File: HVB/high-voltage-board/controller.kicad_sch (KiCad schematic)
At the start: 24 parts, among them J10 Conn_01x05, U4 LD1117S33TR_SOT223, U5 STM32F413CGUx, U6 MCP2551-I-SN, Y1 Crystal

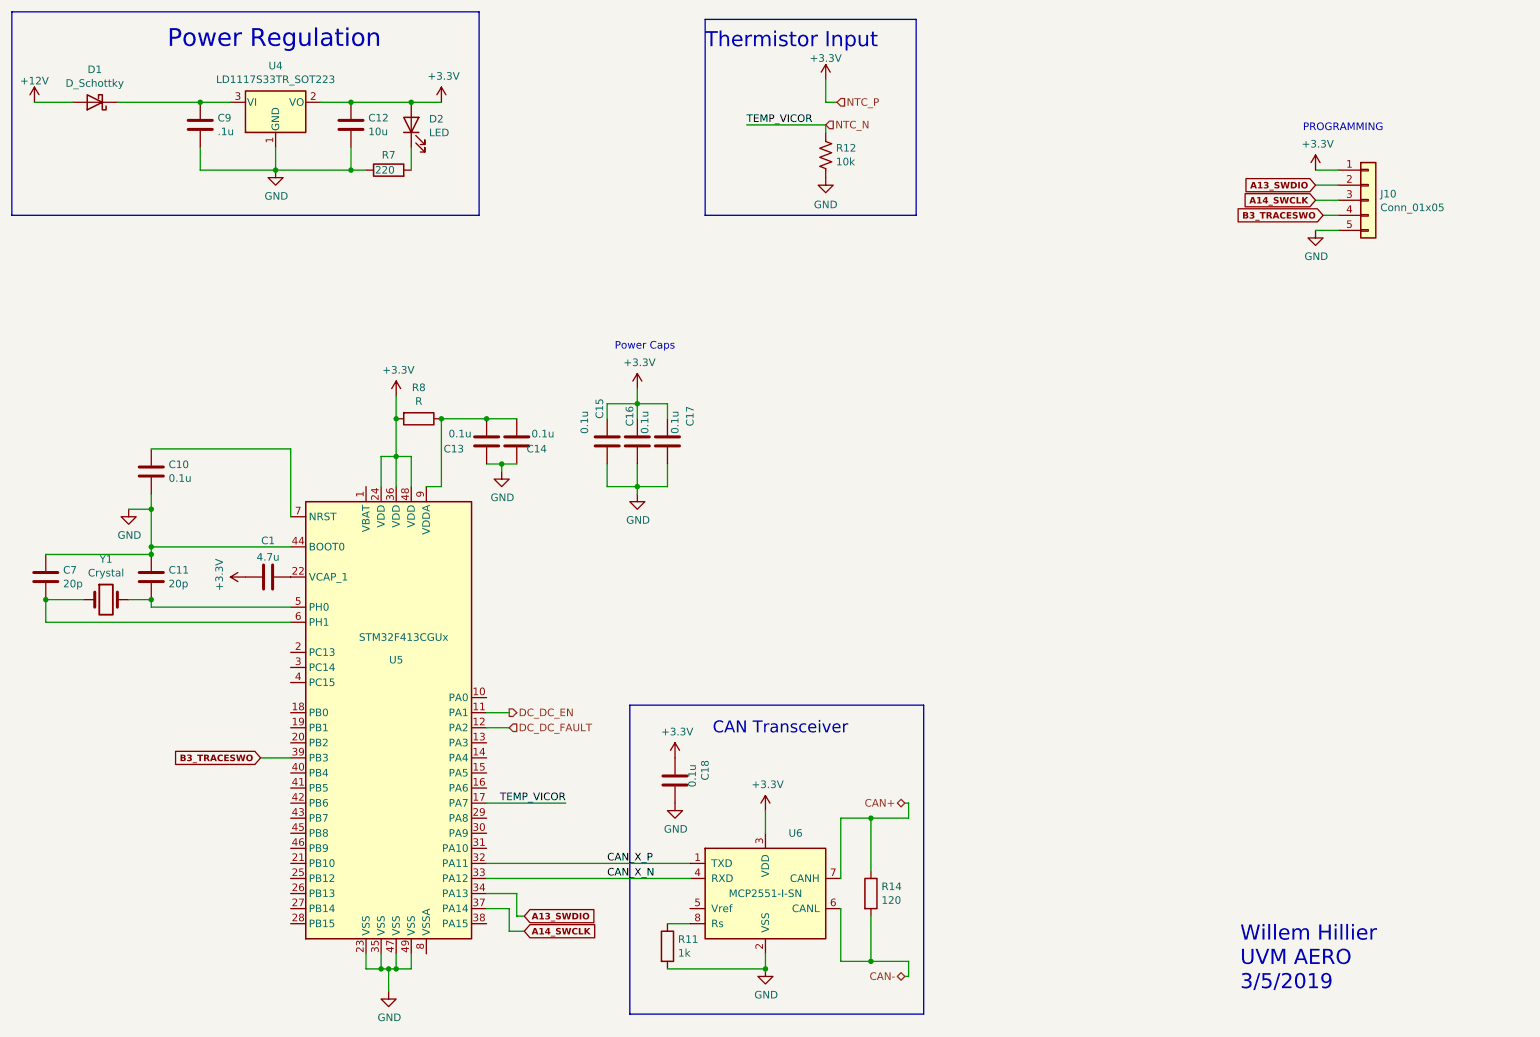
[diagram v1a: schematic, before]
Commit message: Major Review and Part Update
updating footprints, component values, layouts
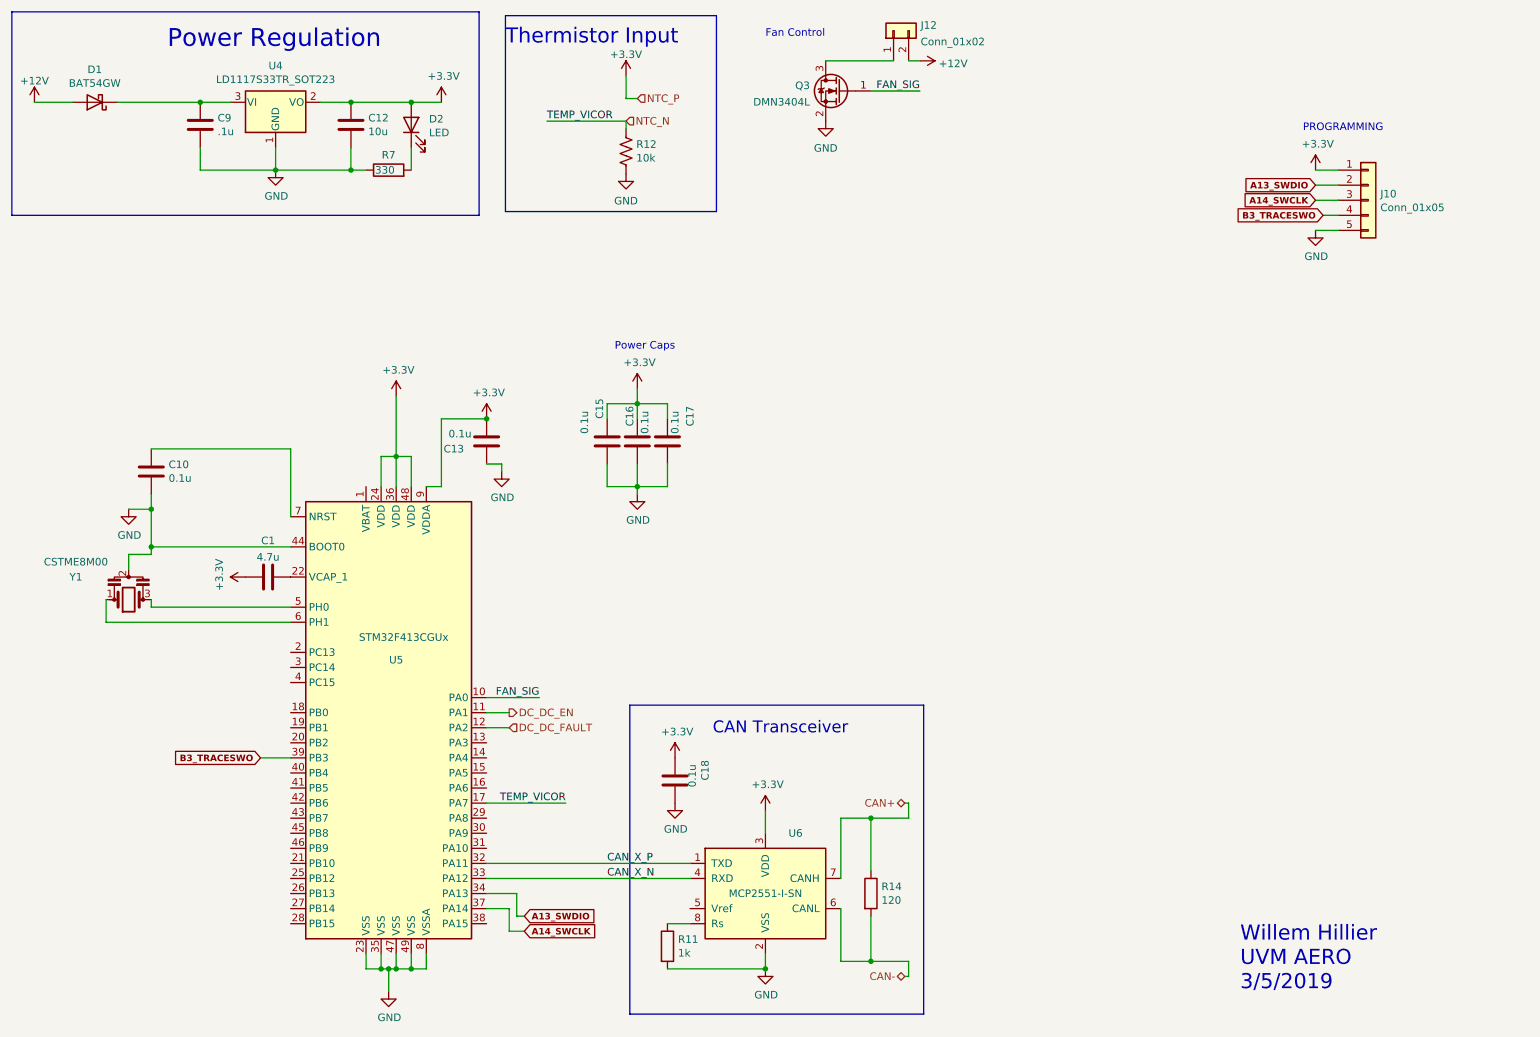
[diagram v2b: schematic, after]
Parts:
- removed C11, C7: 20p, Capacitor_SMD:C_0603_1608Metric_Pad1.08x0.95mm_HandSolder, symbol Device:C
- removed C14: 0.1u, Capacitor_SMD:C_0603_1608Metric_Pad1.08x0.95mm_HandSolder, symbol Device:C
- removed R8: R, Resistor_SMD:R_0603_1608Metric_Pad0.98x0.95mm_HandSolder, symbol Device:R
- removed Y1: Crystal, Crystal:Crystal_HC49-U_Vertical, symbol Device:Crystal
- added J12: Conn_01x02, Connector_JST:JST_XH_B2B-XH-A_1x02_P2.50mm_Vertical, symbol Connector_Generic:Conn_01x02
- added Q3: DMN3404L, Package_TO_SOT_SMD:SOT-23_Handsoldering, symbol Device:Q_NMOS_GSD
- added Y1: CSTME8M00, AERO_Footprints:Resonator_SMD_muRata_CSTxExxV-3Pin_3.0x1.1mm_HandSoldering, symbol Device:Resonator
- D1: value D_Schottky -> BAT54GW; footprint Diode_SMD:D_SMB_Handsoldering -> Diode_SMD:D_SOD-123
- R7: value 220 -> 330
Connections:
- net +12V: now also J12.2 (Pin_2)
- net +3V3: now also C13.2, U5.9 (VDDA)
- net GND: now also U5.8 (VSSA), Q3.2 (S), Y1.2
- net FAN_SIG: now reaches U5.10 (PA0)
- net FAN_SIG: now also Q3.1 (G)
- net at U5.5 (PH0): now also Y1.3
- net at U5.6 (PH1): now also Y1.1
- new net: J12.1 (Pin_1), Q3.3 (D)
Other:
- note added: "Fan Control"
- moved on the sheet: R12

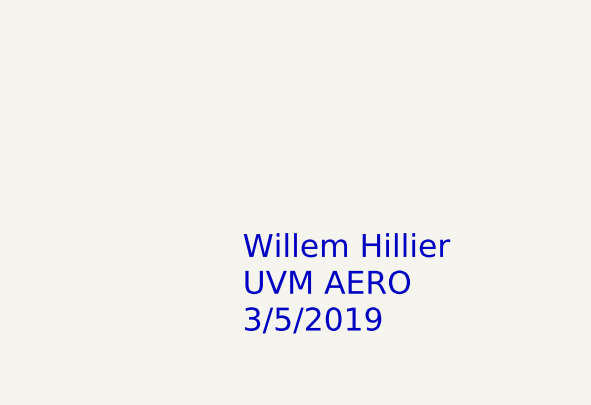
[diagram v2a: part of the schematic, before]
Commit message: updating labels
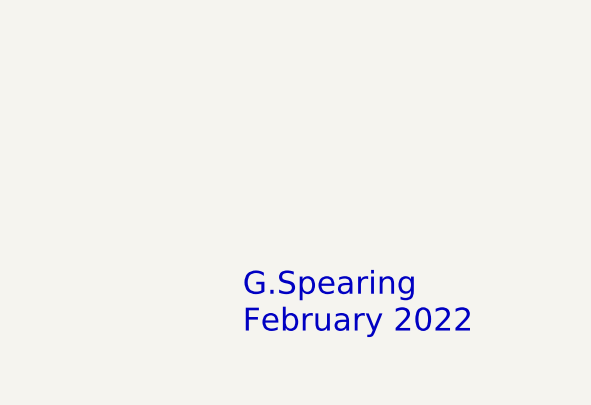
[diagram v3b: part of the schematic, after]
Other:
- note added: "G.Spearing February 2022"
- note removed: "Willem Hillier UVM AERO 3/5/2019"
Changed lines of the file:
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@@
     (stroke (width 0) (type default) (color 0 0 0 0))
   )
-  (text "Willem Hillier\nUVM AERO\n3/5/2019" (at 224.79 179.07 0)
+  (text "G.Spearing\nFebruary 2022" (at 224.79 179.07 0)
     (effects (font (size 2.54 2.54)) (justify left bottom))
   )

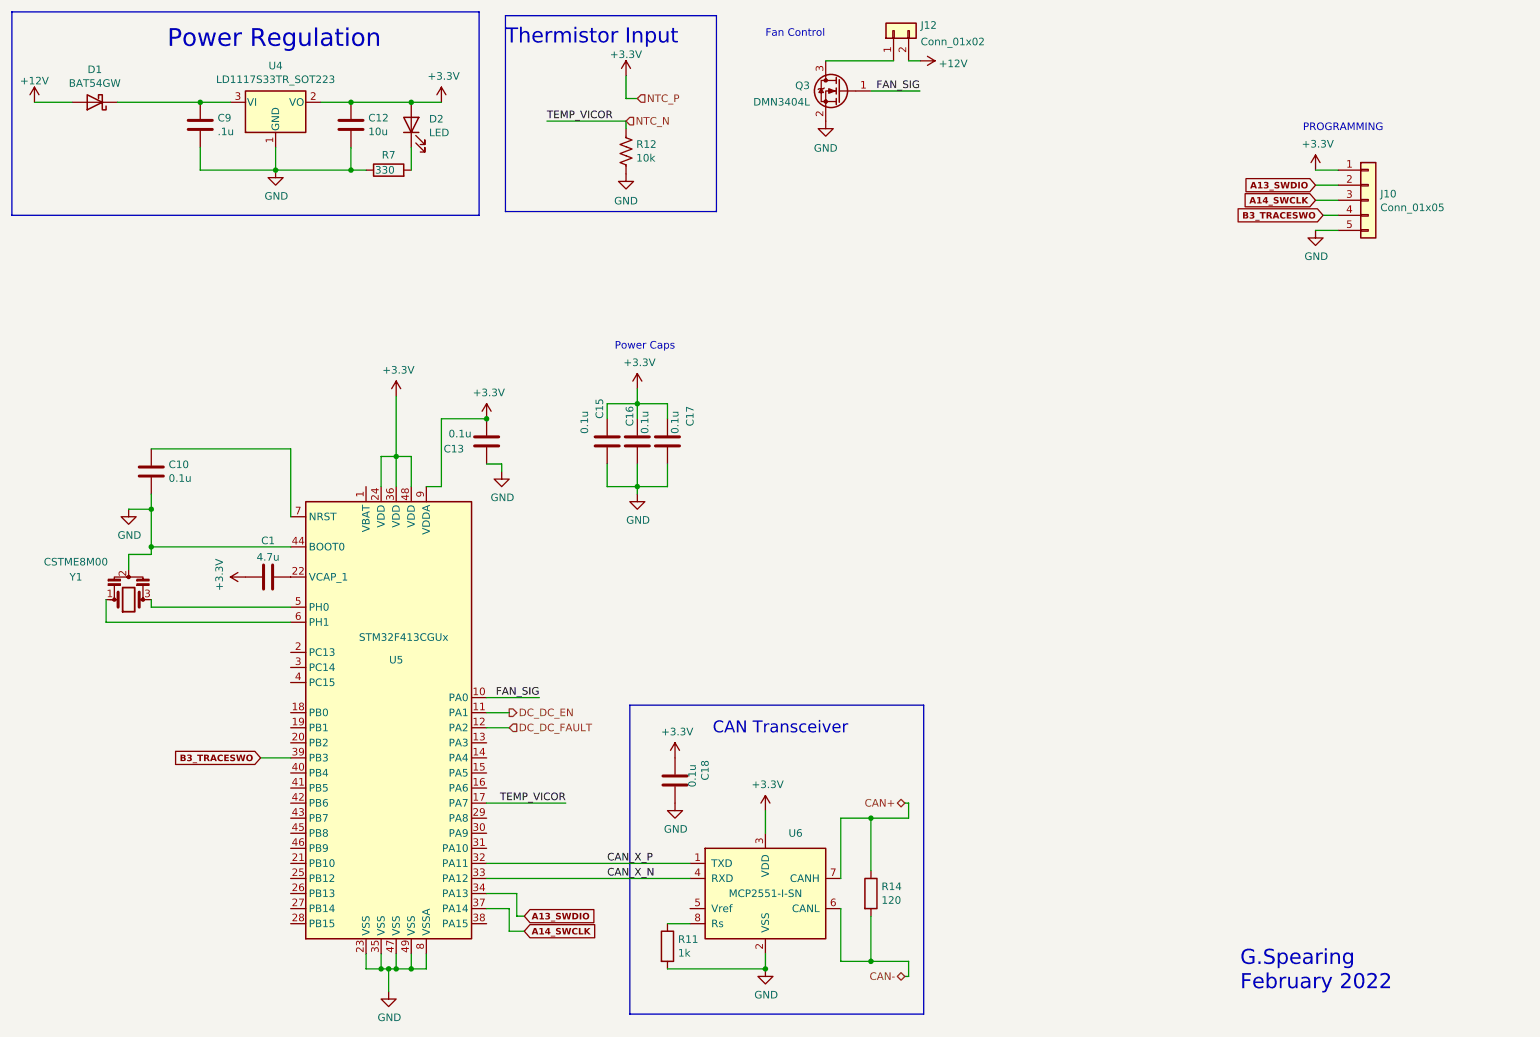
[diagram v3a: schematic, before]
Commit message: adding CAD and changing programming on HVB
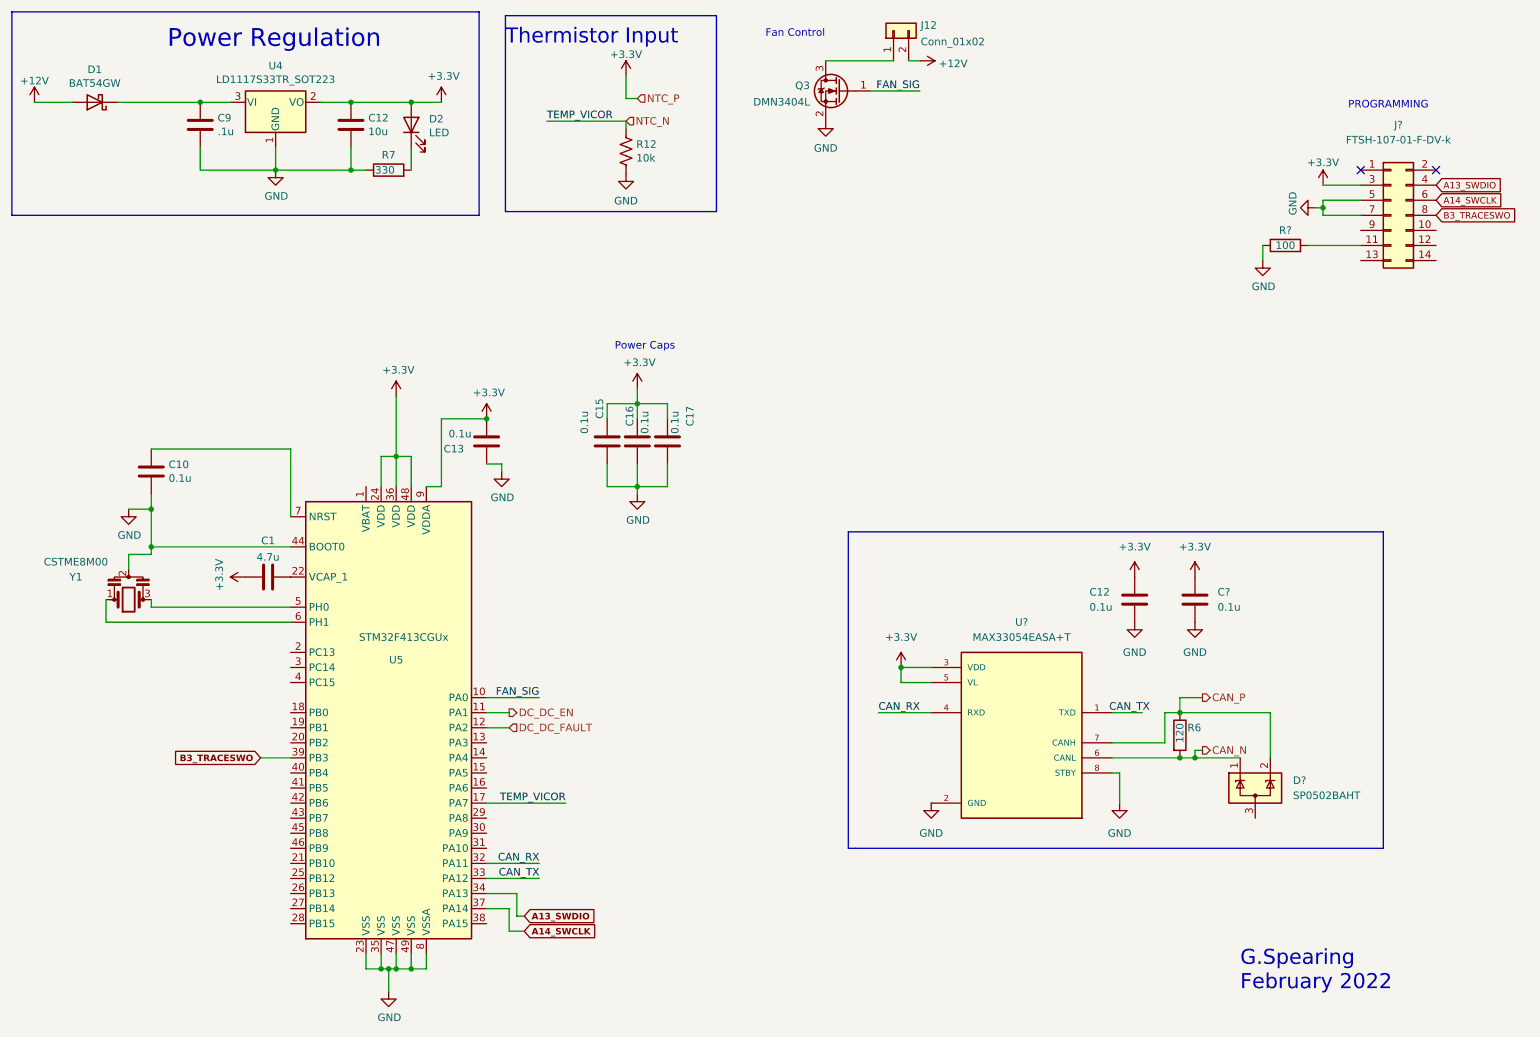
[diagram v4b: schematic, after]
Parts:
- removed C18: 0.1u, Capacitor_SMD:C_0603_1608Metric_Pad1.08x0.95mm_HandSolder, symbol Device:C
- removed J10: Conn_01x05, Connector_JST:JST_XH_B5B-XH-AM_1x05_P2.50mm_Vertical, symbol Connector_Generic:Conn_01x05
- removed R11: 1k, Resistor_SMD:R_0603_1608Metric_Pad0.98x0.95mm_HandSolder, symbol Device:R
- removed R14: 120, Resistor_SMD:R_0603_1608Metric_Pad0.98x0.95mm_HandSolder, symbol Device:R
- removed U6: MCP2551-I-SN, Package_SO:SOIC-8_3.9x4.9mm_P1.27mm, symbol Interface_CAN_LIN:MCP2551-I-SN
- added C12, C?: 0.1u, symbol Device:C
- added D?: SP0502BAHT, Package_TO_SOT_SMD:SOT-23, symbol Power_Protection:SP0502BAHT
- added J?: FTSH-107-01-F-DV-k, symbol Connector_Generic:Conn_02x07_Odd_Even
- added R6: 120, symbol Device:R
- added R?: 100, symbol Device:R
- added U?: MAX33054EASA+T, SOIC127P600X175-8N, symbol AERO_Symbols:MAX33054EASA+T
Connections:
- net +3V3: now also C12.1, C?.1, J?.3 (Pin_3), U?.3 (VDD), U?.5 (VL)
- net A13_SWDIO: now also J?.4 (Pin_4)
- net A14_SWCLK: now also J?.6 (Pin_6)
- net B3_TRACESWO: now also J?.8 (Pin_8)
- net GND: now also C12.2, C?.2, J?.5 (Pin_5), J?.7 (Pin_7), R?.1, U?.2 (GND), U?.8 (STBY)
- net CAN_X_N renamed CAN_TX
- net CAN_X_P renamed CAN_RX
- net CAN_RX: now also U?.4 (RXD)
- new net: J?.11 (Pin_11), R?.2
- new net CAN_N: D?.1 (K), R6.2, U?.6 (CANL)
- new net CAN_P: D?.2 (K), R6.1, U?.7 (CANH)
- no-connect marks 0 -> 2
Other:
- note removed: "CAN Transceiver"
